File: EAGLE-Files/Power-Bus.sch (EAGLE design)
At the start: 13 parts

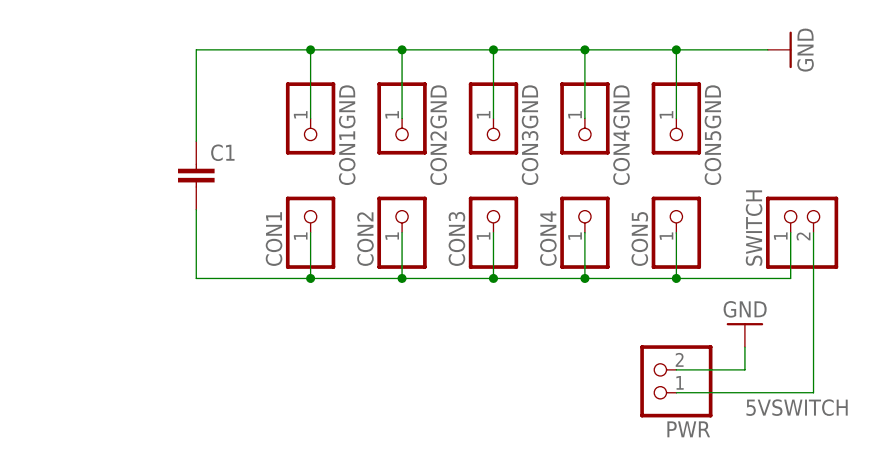
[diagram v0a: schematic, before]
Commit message: Updated all boards for JLCPCB order
Also added the controller boards and schematics back
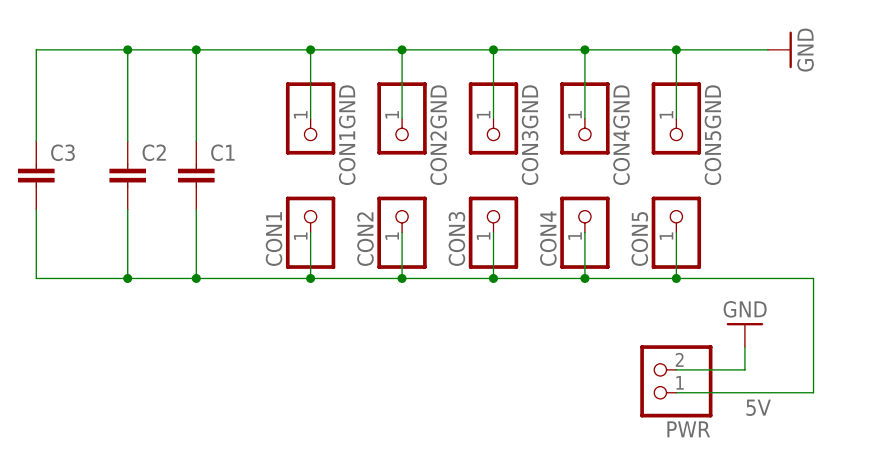
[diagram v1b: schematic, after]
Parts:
- removed SWITCH: (no value), pinhead:PINHD-1X2/90
- added C2, C3: (no value), rcl:C-EU050-025X075
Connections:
- removed net 5VSWITCH: PWR.1, SWITCH.2
- net 5V: now also C2.2, C3.2, PWR.1; no longer SWITCH.1
- net GND: now also C2.1, C3.1
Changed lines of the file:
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@@
 </classes>
 <parts>
-<part name="SWITCH" library="pinhead" library_urn="urn:adsk.eagle:library:325" deviceset="PINHD-1X2" device="/90" package3d_urn="urn:adsk.eagle:package:22437/2"/>
 <part name="PWR" library="pinhead" library_urn="urn:adsk.eagle:library:325" deviceset="PINHD-1X2" device="/90" package3d_urn="urn:adsk.eagle:package:22437/2"/>
 <part name="GND1" library="supply1" library_urn="urn:adsk.eagle:library:371" deviceset="GND" device=""/>
@@
 <part name="GND2" library="supply1" library_urn="urn:adsk.eagle:library:371" deviceset="GND" device=""/>
 <part name="C1" library="rcl" library_urn="urn:adsk.eagle:library:334" deviceset="C-EU" device="050-025X075" package3d_urn="urn:adsk.eagle:package:23637/1"/>
+<part name="C2" library="rcl" library_urn="urn:adsk.eagle:library:334" deviceset="C-EU" device="050-025X075" package3d_urn="urn:adsk.eagle:package:23637/1"/>
+<part name="C3" library="rcl" library_urn="urn:adsk.eagle:library:334" deviceset="C-EU" device="050-025X075" package3d_urn="urn:adsk.eagle:package:23637/1"/>
 </parts>
 <sheets>
@@
 </plain>
 <instances>
-<instance part="SWITCH" gate="G$1" x="66.04" y="60.96" smashed="yes" rot="R90">
-<attribute name="NAME" x="60.325" y="54.61" size="1.778" layer="95" rot="R90"/>
-<attribute name="VALUE" x="71.12" y="54.61" size="1.778" layer="96" rot="R90"/>
-</instance>
 <instance part="PWR" gate="G$1" x="48.26" y="43.18" smashed="yes" rot="R180">
 <attribute name="NAME" x="54.61" y="37.465" size="1.778" layer="95" rot="R180"/>
@@
 <attribute name="VALUE" x="-1.016" y="61.341" size="1.778" layer="96"/>
 </instance>
+<instance part="C2" gate="G$1" x="-10.16" y="66.04" smashed="yes">
+<attribute name="NAME" x="-8.636" y="66.421" size="1.778" layer="95"/>
+<attribute name="VALUE" x="-8.636" y="61.341" size="1.778" layer="96"/>
+</instance>
+<instance part="C3" gate="G$1" x="-20.32" y="66.04" smashed="yes">
+<attribute name="NAME" x="-18.796" y="66.421" size="1.778" layer="95"/>
+<attribute name="VALUE" x="-18.796" y="61.341" size="1.778" layer="96"/>
+</instance>
 </instances>
 <busses>
 </busses>
 <nets>
-<net name="5VSWITCH" class="0">
-<segment>
-<pinref part="PWR" gate="G$1" pin="1"/>
-<wire x1="66.04" y1="40.64" x2="50.8" y2="40.64" width="0.1524" layer="91"/>
-<pinref part="SWITCH" gate="G$1" pin="2"/>
-<wire x1="66.04" y1="58.42" x2="66.04" y2="40.64" width="0.1524" layer="91"/>
-<label x="58.42" y="38.1" size="1.778" layer="95"/>
-</segment>
-</net>
 <net name="GND" class="0">
 <segment>
@@
 <wire x1="-2.54" y1="78.74" x2="-2.54" y2="68.58" width="0.1524" layer="91"/>
 <junction x="10.16" y="78.74"/>
+<pinref part="C2" gate="G$1" pin="1"/>
+<wire x1="-10.16" y1="68.58" x2="-10.16" y2="78.74" width="0.1524" layer="91"/>
+<wire x1="-10.16" y1="78.74" x2="-2.54" y2="78.74" width="0.1524" layer="91"/>
+<junction x="-2.54" y="78.74"/>
+<pinref part="C3" gate="G$1" pin="1"/>
+<wire x1="-20.32" y1="68.58" x2="-20.32" y2="78.74" width="0.1524" layer="91"/>
+<wire x1="-20.32" y1="78.74" x2="-10.16" y2="78.74" width="0.1524" layer="91"/>
+<junction x="-10.16" y="78.74"/>
 </segment>
 </net>
 <net name="5V" class="0">
 <segment>
-<pinref part="SWITCH" gate="G$1" pin="1"/>
-<wire x1="63.5" y1="58.42" x2="63.5" y2="53.34" width="0.1524" layer="91"/>
 <pinref part="CON5" gate="G$1" pin="1"/>
 <wire x1="50.8" y1="58.42" x2="50.8" y2="53.34" width="0.1524" layer="91"/>
-<wire x1="50.8" y1="53.34" x2="63.5" y2="53.34" width="0.1524" layer="91"/>
+<wire x1="50.8" y1="53.34" x2="66.04" y2="53.34" width="0.1524" layer="91"/>
 <pinref part="CON4" gate="G$1" pin="1"/>
 <wire x1="50.8" y1="53.34" x2="40.64" y2="53.34" width="0.1524" layer="91"/>
@@
 <wire x1="-2.54" y1="53.34" x2="10.16" y2="53.34" width="0.1524" layer="91"/>
 <junction x="10.16" y="53.34"/>
+<pinref part="PWR" gate="G$1" pin="1"/>
+<wire x1="66.04" y1="40.64" x2="50.8" y2="40.64" width="0.1524" layer="91"/>
+<label x="58.42" y="38.1" size="1.778" layer="95"/>
+<wire x1="66.04" y1="53.34" x2="66.04" y2="40.64" width="0.1524" layer="91"/>
+<pinref part="C2" gate="G$1" pin="2"/>
+<wire x1="-2.54" y1="53.34" x2="-10.16" y2="53.34" width="0.1524" layer="91"/>
+<wire x1="-10.16" y1="53.34" x2="-10.16" y2="60.96" width="0.1524" layer="91"/>
+<junction x="-2.54" y="53.34"/>
+<pinref part="C3" gate="G$1" pin="2"/>
+<wire x1="-10.16" y1="53.34" x2="-20.32" y2="53.34" width="0.1524" layer="91"/>
+<wire x1="-20.32" y1="53.34" x2="-20.32" y2="60.96" width="0.1524" layer="91"/>
+<junction x="-10.16" y="53.34"/>
 </segment>
 </net>
